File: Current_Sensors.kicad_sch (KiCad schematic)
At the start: 12 parts

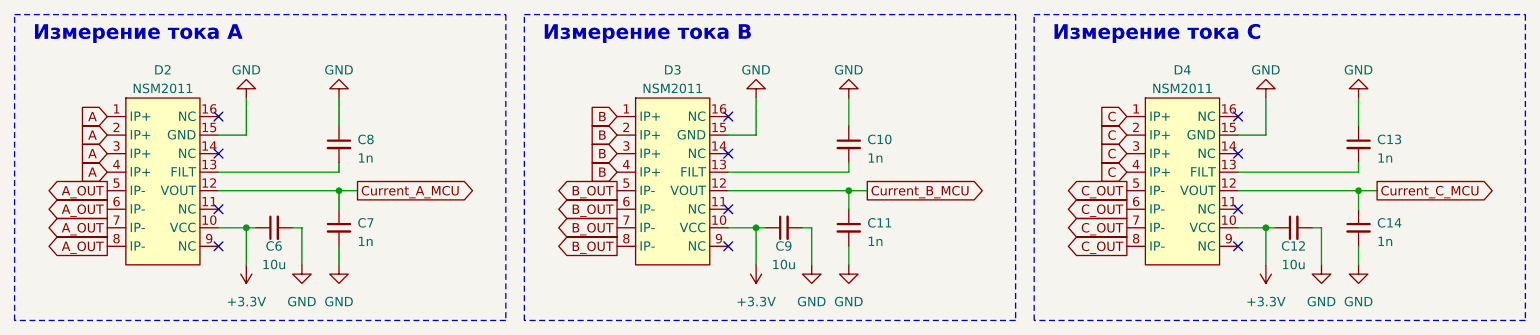
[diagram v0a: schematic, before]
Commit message: Поменял датчики на шунты
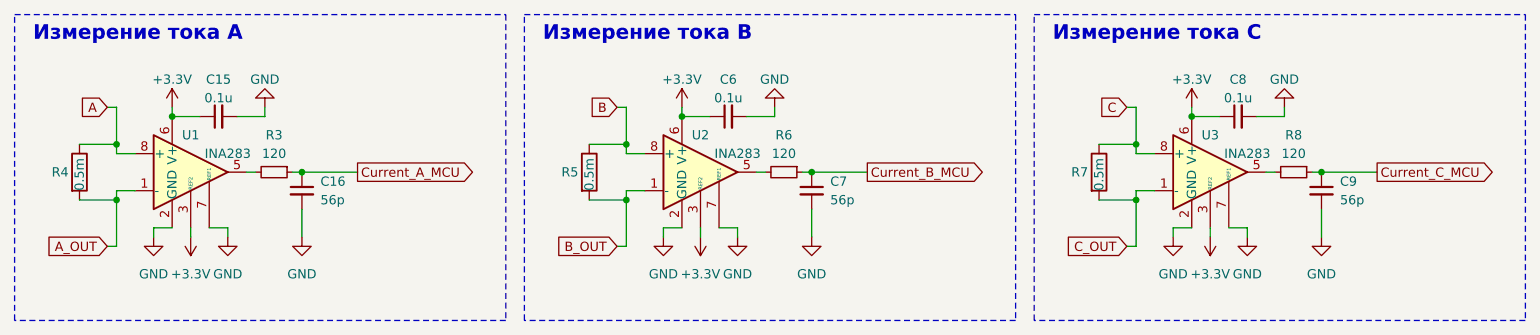
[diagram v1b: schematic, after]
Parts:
- removed C10, C11, C13, C14: 1n, Capacitor_SMD:C_0603_1608Metric_Pad1.08x0.95mm_HandSolder, symbol Device:C_Small
- removed C12: 10u, Capacitor_SMD:C_0603_1608Metric_Pad1.08x0.95mm_HandSolder, symbol Device:C_Small
- removed D2, D3, D4: NSM2011, Package_SO:SOIC-16W_7.5x10.3mm_P1.27mm, symbol Sensors_My:NSM2011
- added C15: 0.1u, Capacitor_SMD:C_0603_1608Metric_Pad1.08x0.95mm_HandSolder, symbol Device:C_Small
- added C16: 56p, Capacitor_SMD:C_0603_1608Metric_Pad1.08x0.95mm_HandSolder, symbol Device:C_Small
- added R3, R6, R8: 120, Resistor_SMD:R_0603_1608Metric_Pad0.98x0.95mm_HandSolder, symbol Device:R_Small
- added R4, R5, R7: 0.5m, Resistor_SMD:R_2512_6332Metric_Pad1.40x3.35mm_HandSolder, symbol Device:R
- added U1, U2, U3: INA283, Package_SO:SOIC-8_3.9x4.9mm_P1.27mm, symbol Amplifier_Current:INA283
- C6: value 10u -> 0.1u
- C7: value 1n -> 56p
- C8: value 1n -> 0.1u
- C9: value 10u -> 56p
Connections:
- net +3.3V: now also C8.1, C15.1, U1.3 (REF2), U1.6 (V+), U2.3 (REF2), U2.6 (V+), U3.3 (REF2), U3.6 (V+); no longer C9.1
- net A: now also R4.1, U1.8 (+)
- net A_OUT: now also R4.2, U1.1 (-)
- net B: now also R5.1, U2.8 (+)
- net B_OUT: now also R5.2, U2.1 (-)
- net C: now also R7.1, U3.8 (+)
- net C_OUT: now also R7.2, U3.1 (-)
- net Current_A_MCU: now also C16.1, R3.1; no longer C7.1
- net Current_B_MCU: now also C7.1, R6.1
- net Current_C_MCU: now also C9.1, R8.1
- net GND: now also C8.2, C15.2, C16.2, U1.2 (GND), U1.7 (REF1), U2.2 (GND), U2.7 (REF1), U3.2 (GND), U3.7 (REF1); no longer C8.1
- new net: R8.2, U3.5
- new net: R3.2, U1.5
- new net: R6.2, U2.5
- no-connect marks 12 -> 0
